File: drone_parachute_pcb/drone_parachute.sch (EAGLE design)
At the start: 33 parts, among them T1 BC547, U1 GY-521MPU6050, U2 AMS1117-3.3

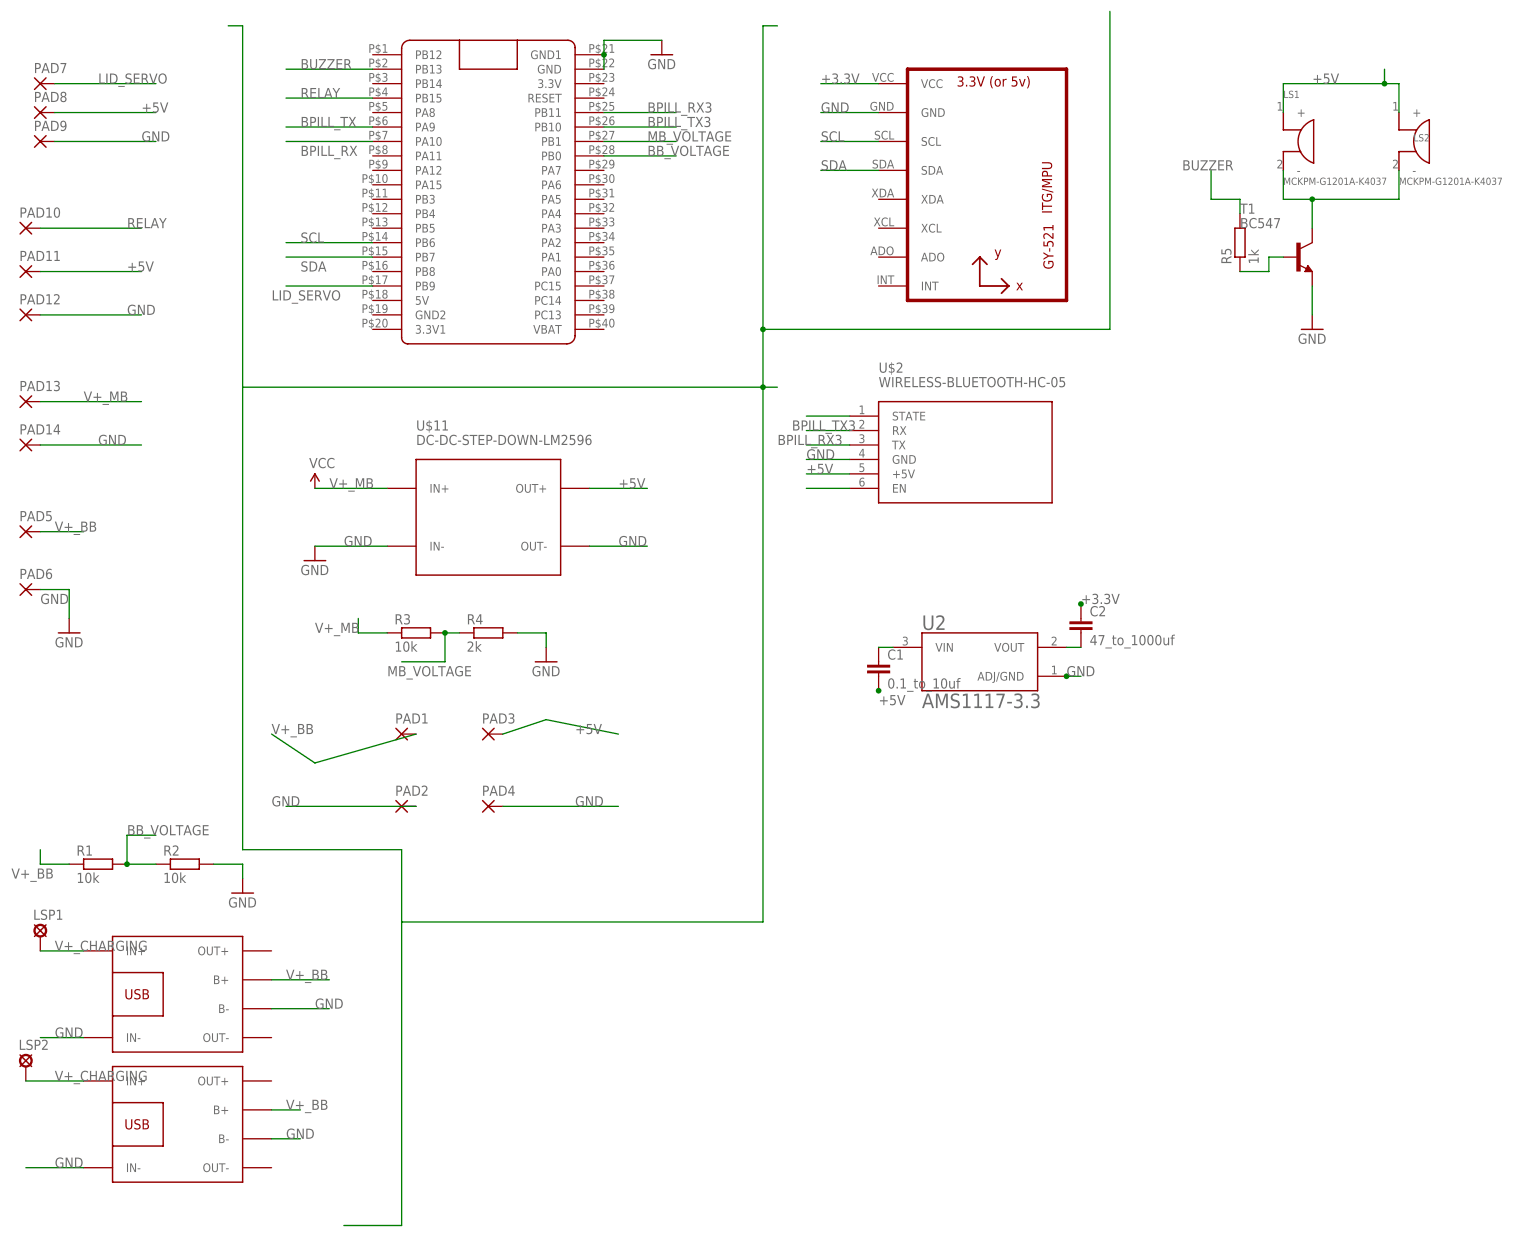
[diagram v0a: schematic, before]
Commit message: added Ti's charging IC schematic.
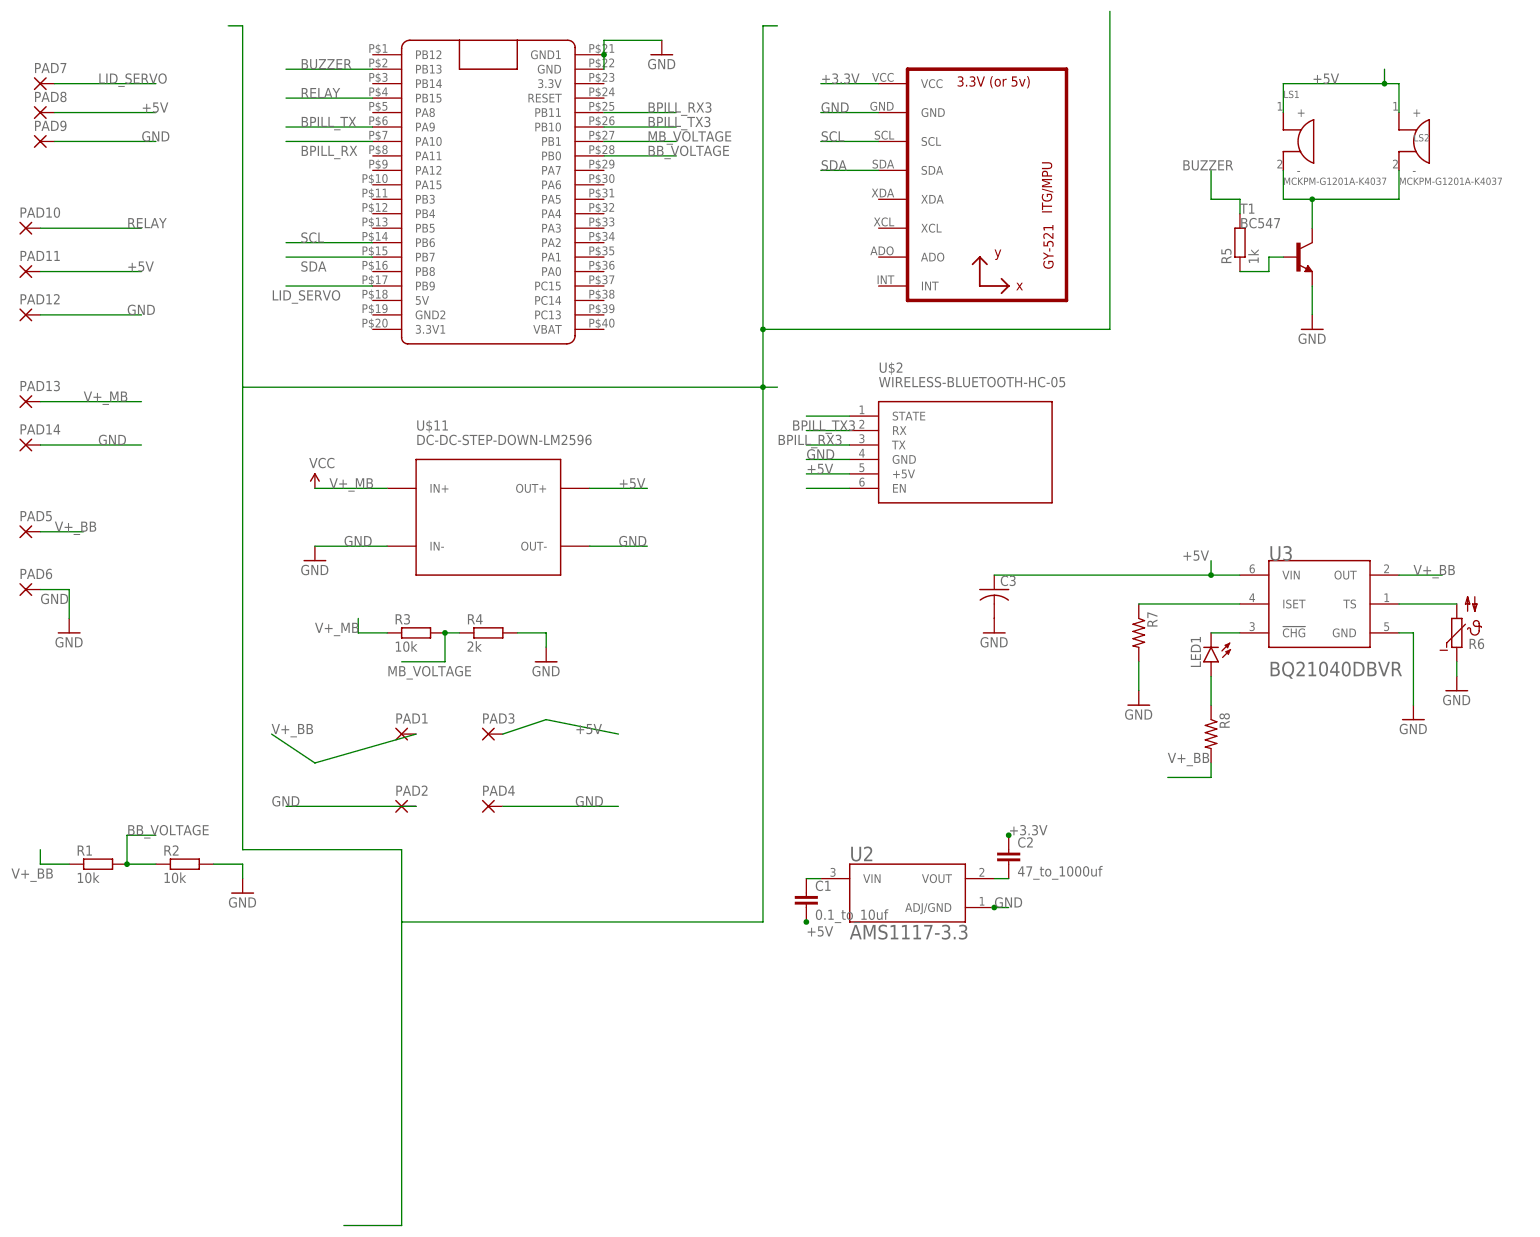
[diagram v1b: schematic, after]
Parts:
- removed LSP1, LSP2: LSP10, solpad:LSP10
- removed U$7, U$8: BATTERY-CHARGER-LI-PROT, diy-modules:BATTERY-CHARGER-LI-PROT
- added C3: (no value), rcl:C-USC0805
- added LED1: (no value), led:LEDCHIP-LED0805
- added R6: (no value), ptc-ntc:NTC640
- added R7, R8: (no value), rcl:R-US_R0805
- added U3: TEXAS_INSTRUMENTS_BQ21040DBVRTEXAS_INSTRUMENTS_BQ21040DBVR_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, Texas Instruments - BQ21040DBVR:TEXAS_INSTRUMENTS_BQ21040DBVRTEXAS_INSTRUMENTS_BQ21040DBVR_0_0
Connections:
- removed net V+_CHARGING: LSP1.MP, LSP2.MP, U$7.IN+, U$8.IN+
- new net N$11: R7.1, U3.ISET
- new net N$13: LED1.A, R8.1
- new net N$7: R6.2, U3.TS
- new net N$9: LED1.C, U3.!CHG!
- net +5V: now also C3.1, U3.VIN
- net GND: now also C3.2, R6.1, R7.2, U3.GND; no longer U$7.B-, U$7.IN-, U$8.B-, U$8.IN-
- net V+_BB: now also R8.2, U3.OUT; no longer U$7.B+, U$8.B+
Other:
- moved on the sheet: C1, C2, U2

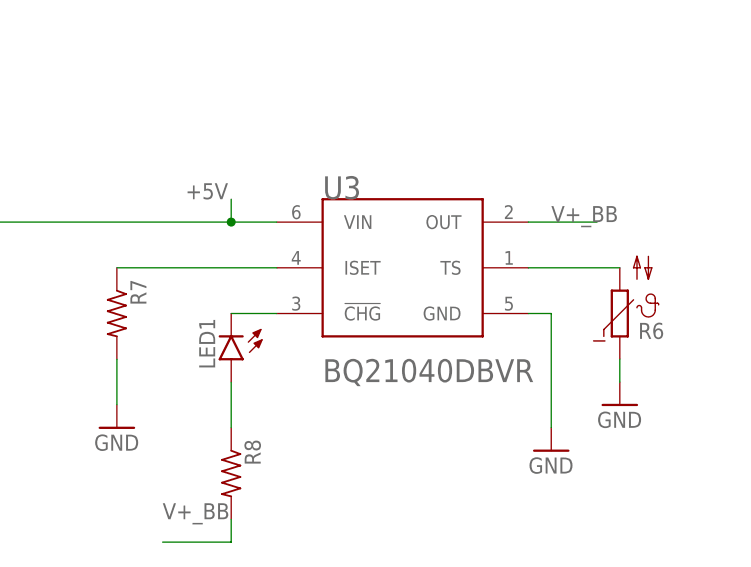
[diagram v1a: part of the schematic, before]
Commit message: added board .brd for charging IC.
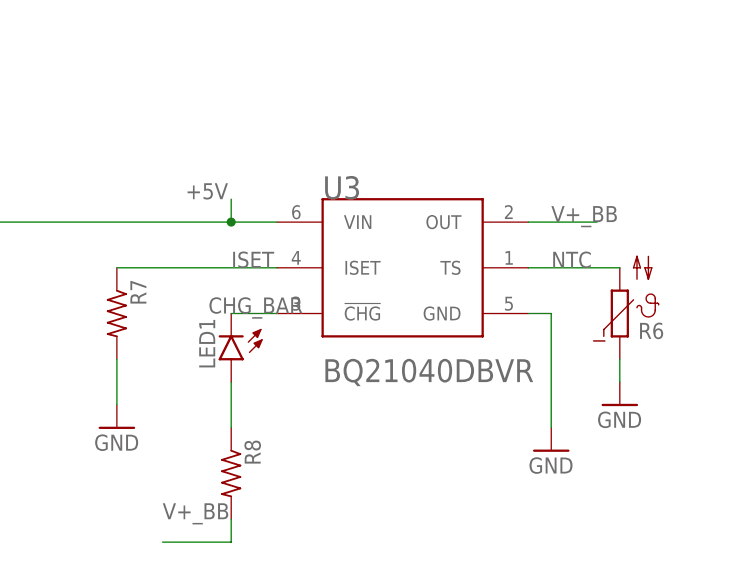
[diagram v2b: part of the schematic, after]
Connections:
- net N$11 renamed ISET
- net N$7 renamed NTC
- net N$9 renamed CHG_BAR
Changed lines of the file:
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@@
 <?xml version="1.0" encoding="utf-8"?>
 <!DOCTYPE eagle SYSTEM "eagle.dtd">
-<eagle version="9.5.2">
+<eagle version="9.5.0">
 <drawing>
 <settings>
@@
 </segment>
 </net>
-<net name="N$7" class="0">
+<net name="NTC" class="0">
 <segment>
 <pinref part="U3" gate="G$0" pin="TS"/>
 <wire x1="254" y1="109.22" x2="264.16" y2="109.22" width="0.1524" layer="91"/>
 <pinref part="R6" gate="1" pin="2"/>
-</segment>
-</net>
-<net name="N$9" class="0">
+<label x="256.54" y="109.22" size="1.778" layer="95"/>
+</segment>
+</net>
+<net name="CHG_BAR" class="0">
 <segment>
 <pinref part="U3" gate="G$0" pin="!CHG!"/>
 <wire x1="226.06" y1="104.14" x2="220.98" y2="104.14" width="0.1524" layer="91"/>
 <pinref part="LED1" gate="G$1" pin="C"/>
-</segment>
-</net>
-<net name="N$11" class="0">
+<label x="218.44" y="104.14" size="1.778" layer="95"/>
+</segment>
+</net>
+<net name="ISET" class="0">
 <segment>
 <pinref part="U3" gate="G$0" pin="ISET"/>
 <pinref part="R7" gate="G$1" pin="1"/>
 <wire x1="208.28" y1="109.22" x2="226.06" y2="109.22" width="0.1524" layer="91"/>
-</segment>
-</net>
+<label x="220.98" y="109.22" size="1.778" layer="95"/>
+</segment>
+</net>
